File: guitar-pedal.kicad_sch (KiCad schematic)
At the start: 50 parts, among them J1 USB_OTG, J2 AudioJack2, J3 AudioJack2, J4 Test_Headers, SW1 SW_SPDT, SW2 SW_3PDT, SW3 Boot, SW4 Reset, SW5 SW_Push_SPDT, SW6 SW_Push_SPDT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

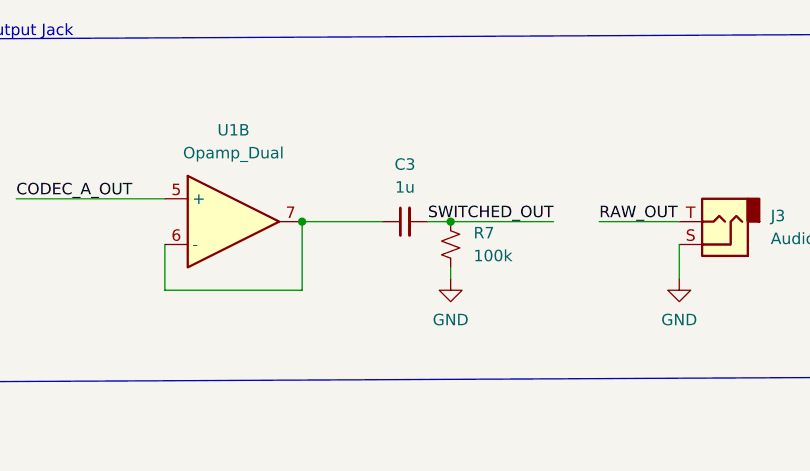
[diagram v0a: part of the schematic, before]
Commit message: add missing letter F from capacitor value
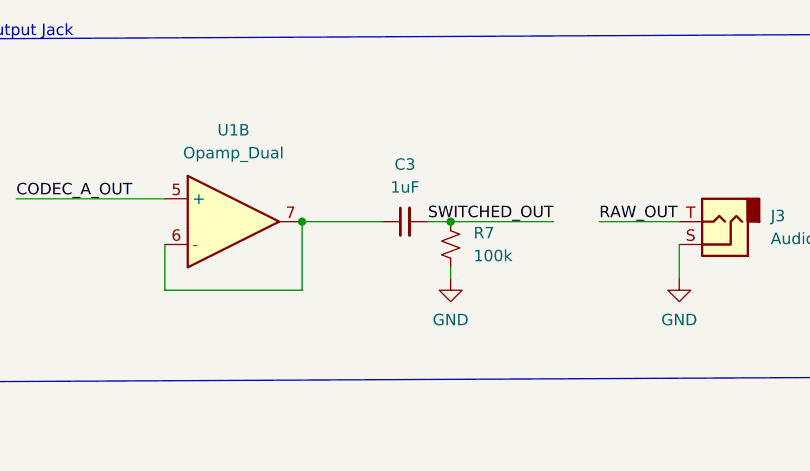
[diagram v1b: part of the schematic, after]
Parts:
- C3: value 1u -> 1uF
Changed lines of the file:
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@@
     (in_bom yes) (on_board yes) (fields_autoplaced)
     (property "Reference" "C3" (id 0) (at 217.1763 38.1 90))
-    (property "Value" "1u" (id 1) (at 217.1763 40.64 90))
+    (property "Value" "1uF" (id 1) (at 217.1763 40.64 90))
     (property "Footprint" "" (id 2) (at 217.17 44.45 0)
       (effects (font (size 1.27 1.27)) hide)
@@
     )
     (path "/5098fff7-b1bd-4ef1-99fe-3f3750157a32"
-      (reference "C3") (unit 1) (value "1u") (footprint "")
+      (reference "C3") (unit 1) (value "1uF") (footprint "")
     )
     (path "/2b35be39-6c74-45b8-a4e7-272df3c08333"

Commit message: some reorganization
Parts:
- gave numbers to parts that had none: 1
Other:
- moved on the sheet: C1, C10, C12, C15, C16, C17, C18, C19, C20, C21, C22, C23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

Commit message: assign footprints and fix a couple small things
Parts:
- C1, C11, C12, C13, C14, C16, C18, C19, C20, C22, C3, C4, C5, C7, C8: footprint (none) -> Capacitor_SMD:C_0603_1608Metric_Pad1.08x0.95mm_HandSolder
- C10, C9: value 10uF -> 1uF; footprint (none) -> Capacitor_SMD:C_0603_1608Metric_Pad1.08x0.95mm_HandSolder
- C15, C17, C6: footprint (none) -> Capacitor_SMD:C_0805_2012Metric_Pad1.18x1.45mm_HandSolder
- C21: value 4.7uF -> 1uF; footprint (none) -> Capacitor_SMD:C_0603_1608Metric_Pad1.08x0.95mm_HandSolder; symbol Device:C_Polarized_Small_US -> Device:C_Small
- C23: footprint (none) -> Capacitor_SMD:C_0805_2012Metric_Pad1.18x1.45mm_HandSolder; symbol Device:C_Small -> Device:C_Polarized_Small_US
- C24: footprint (none) -> Capacitor_SMD:C_0603_1608Metric_Pad1.08x0.95mm_HandSolder; symbol Device:C_Small -> Device:C_Polarized_Small_US
- D1, POT1, POT2, POT3, POT4, POT5, POT6, SW1, SW5, SW6: footprint (none) -> Connector_PinHeader_2.54mm:PinHeader_1x03_P2.54mm_Vertical
- J1: footprint (none) -> Connector_USB:USB_Micro-B_Molex-105017-0001
- J2, J3, SW4: footprint (none) -> Connector_PinHeader_2.54mm:PinHeader_1x02_P2.54mm_Vertical
- J4: footprint (none) -> Connector_PinHeader_2.54mm:PinHeader_1x10_P2.54mm_Vertical
- R1, R3, R5, R7, R9, SW3: footprint (none) -> Resistor_SMD:R_0603_1608Metric_Pad0.98x0.95mm_HandSolder
- R8: footprint (none) -> Resistor_SMD:R_0805_2012Metric_Pad1.20x1.40mm_HandSolder
- SW2: footprint (none) -> Connector_PinHeader_2.54mm:PinHeader_1x09_P2.54mm_Vertical
- U1: footprint (none) -> RC4580IPWR:PW8
- U4: renamed from PCM3002E1; footprint (none) -> PCM3002E:PCM3002E
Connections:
- net +3V3: now also C23.1; no longer C23.2
- net GND: now also C23.2; no longer C23.1

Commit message: getting started on layout
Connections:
- net GND: now also J2.1 (S), J3.1 (S); no longer J2.S, J3.S
- net RAW_IN: now also J2.2 (T); no longer J2.T
- net RAW_OUT: now also J3.2 (T); no longer J3.T
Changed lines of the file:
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@@
     (effects (font (size 1.27 1.27)) (justify left bottom))
   )
-  (symbol (lib_id "Connector:AudioJack2") (at 67.945 36.83 90) (mirror x) (unit 1)
-    (in_bom yes) (on_board yes) (fields_autoplaced)
-    (property "Reference" "J2" (id 0) (at 71.755 34.9249 90)
-      (effects (font (size 1.27 1.27)) (justify right))
-    )
-    (property "Value" "AudioJack2" (id 1) (at 71.755 37.4649 90)
+  (symbol (lib_name "AudioJack2_1") (lib_id "Connector:AudioJack2") (at 67.945 36.83 90) (mirror x) (unit 1)
+    (in_bom yes) (on_board yes)
+    (property "Reference" "J2" (id 0) (at 66.802 29.464 90)
+      (effects (font (size 1.27 1.27)) (justify right))
+    )
+    (property "Value" "AudioJack2" (id 1) (at 62.484 31.496 90)
       (effects (font (size 1.27 1.27)) (justify right))
     )
@@
       (effects (font (size 1.27 1.27)) hide)
     )
-    (pin "S")
-    (pin "T")
+    (pin "2")
+    (pin "1")
   )
   (symbol (lib_id "Switch:SW_Push") (at 271.78 105.918 0) (unit 1)
@@
   )
   (symbol (lib_id "Connector:AudioJack2") (at 255.905 44.45 180) (unit 1)
-    (in_bom yes) (on_board yes) (fields_autoplaced)
-    (property "Reference" "J3" (id 0) (at 260.985 43.8149 0)
-      (effects (font (size 1.27 1.27)) (justify right))
-    )
-    (property "Value" "AudioJack2" (id 1) (at 260.985 46.3549 0)
+    (in_bom yes) (on_board yes)
+    (property "Reference" "J3" (id 0) (at 254.762 38.1 0)
+      (effects (font (size 1.27 1.27)) (justify right))
+    )
+    (property "Value" "AudioJack2" (id 1) (at 250.444 40.132 0)
       (effects (font (size 1.27 1.27)) (justify right))
     )
@@
       (effects (font (size 1.27 1.27)) hide)
     )
-    (pin "S")
-    (pin "T")
+    (pin "1")
+    (pin "2")
   )
   (symbol (lib_id "power:+3V3") (at 238.506 103.632 0) (unit 1)

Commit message: no seriously, get started on layout
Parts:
- J4: footprint Connector_PinHeader_2.54mm:PinHeader_1x10_P2.54mm_Vertical -> Connector_PinHeader_2.54mm:PinHeader_2x05_P2.54mm_Vertical
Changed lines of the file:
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@@
       (effects (font (size 1.27 1.27)) (justify right))
     )
-    (property "Footprint" "Connector_PinHeader_2.54mm:PinHeader_1x10_P2.54mm_Vertical" (id 2) (at 346.202 91.948 0)
+    (property "Footprint" "Connector_PinHeader_2.54mm:PinHeader_2x05_P2.54mm_Vertical" (id 2) (at 346.202 91.948 0)
       (effects (font (size 1.27 1.27)) hide)
     )
@@
     )
     (path "/8b87fcfc-4d33-4e63-b56b-68b24da21f98"
-      (reference "J4") (unit 1) (value "Test_Headers") (footprint "Connector_PinHeader_2.54mm:PinHeader_1x10_P2.54mm_Vertical")
+      (reference "J4") (unit 1) (value "Test_Headers") (footprint "Connector_PinHeader_2.54mm:PinHeader_2x05_P2.54mm_Vertical")
     )
     (path "/d150c883-e641-4548-a17d-a4c8e8775a90"

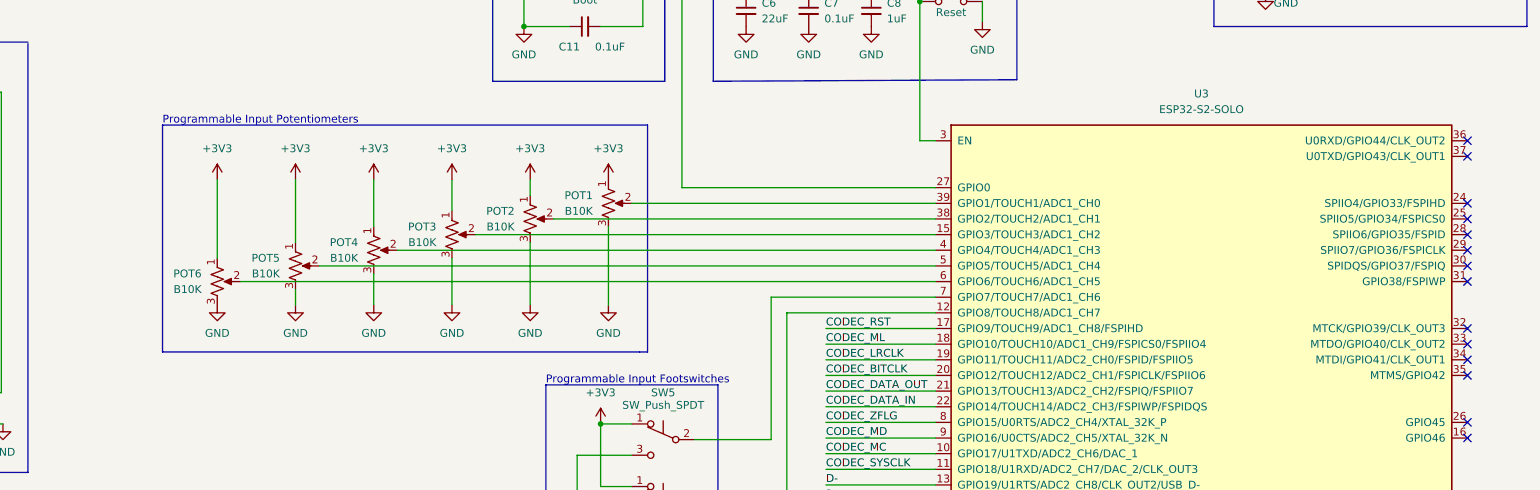
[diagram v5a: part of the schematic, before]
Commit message: Reassign potentiometer pins to esp32
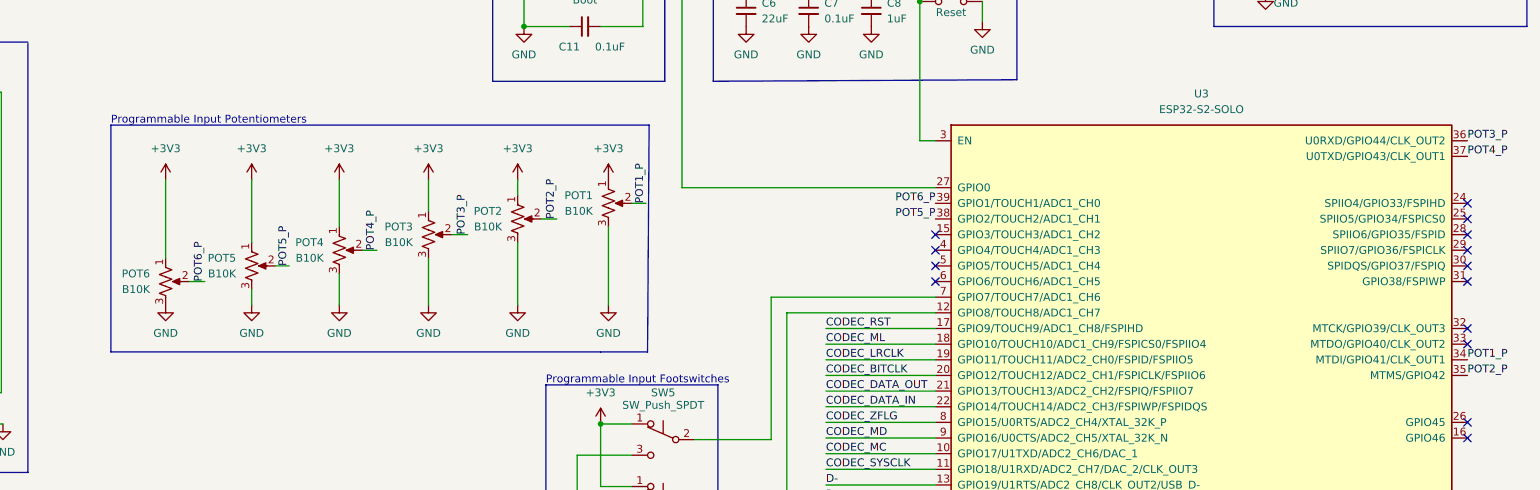
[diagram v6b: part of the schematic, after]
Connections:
- net at U3.4 (GPIO4/TOUCH4/ADC1_CH3): no longer POT4.2
- net at U3.15 (GPIO3/TOUCH3/ADC1_CH2): no longer POT3.2
- net at U3.6 (GPIO6/TOUCH6/ADC1_CH5): no longer POT6.2
- net POT1_P: now reaches POT1.2
- net POT1_P: now also U3.34 (MTDI/GPIO41/CLK_OUT1); no longer U3.39 (GPIO1/TOUCH1/ADC1_CH0)
- net POT2_P: now reaches U3.35 (MTMS/GPIO42)
- net POT2_P: now also POT2.2
- net POT3_P: now reaches U3.36 (U0RXD/GPIO44/CLK_OUT2)
- net POT3_P: now also POT3.2
- net POT4_P: now reaches U3.37 (U0TXD/GPIO43/CLK_OUT1)
- net POT4_P: now also POT4.2
- net POT5_P: now reaches U3.38 (GPIO2/TOUCH2/ADC1_CH1)
- net POT5_P: now also POT5.2; no longer POT2.2
- net at U3.5 (GPIO5/TOUCH5/ADC1_CH4): no longer POT5.2
- new net POT6_P: POT6.2, U3.39 (GPIO1/TOUCH1/ADC1_CH0)
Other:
- moved on the sheet: POT2, POT3, POT4, POT5, POT6

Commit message: layout progress!
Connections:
- net CODEC_BITCLK: now also U3.18 (GPIO10/TOUCH10/ADC1_CH9/FSPICS0/FSPIIO4); no longer U3.20 (GPIO12/TOUCH12/ADC2_CH1/FSPICLK/FSPIIO6)
- net CODEC_DATA_IN: now also U3.11 (GPIO18/U1RXD/ADC2_CH7/DAC_2/CLK_OUT3); no longer U3.22 (GPIO14/TOUCH14/ADC2_CH3/FSPIWP/FSPIDQS)
- net CODEC_DATA_OUT: now also U3.17 (GPIO9/TOUCH9/ADC1_CH8/FSPIHD); no longer U3.21 (GPIO13/TOUCH13/ADC2_CH2/FSPIQ/FSPIIO7)
- net CODEC_MC: now also U3.8 (GPIO15/U0RTS/ADC2_CH4/XTAL_32K_P); no longer U3.10 (GPIO17/U1TXD/ADC2_CH6/DAC_1)
- net CODEC_ML: now also U3.21 (GPIO13/TOUCH13/ADC2_CH2/FSPIQ/FSPIIO7); no longer U3.18 (GPIO10/TOUCH10/ADC1_CH9/FSPICS0/FSPIIO4)
- net CODEC_RST: now also U3.22 (GPIO14/TOUCH14/ADC2_CH3/FSPIWP/FSPIDQS); no longer U3.17 (GPIO9/TOUCH9/ADC1_CH8/FSPIHD)
- net CODEC_SYSCLK: now also U3.20 (GPIO12/TOUCH12/ADC2_CH1/FSPICLK/FSPIIO6); no longer U3.11 (GPIO18/U1RXD/ADC2_CH7/DAC_2/CLK_OUT3)
- net CODEC_ZFLG: now also U3.10 (GPIO17/U1TXD/ADC2_CH6/DAC_1); no longer U3.8 (GPIO15/U0RTS/ADC2_CH4/XTAL_32K_P)
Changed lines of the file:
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@@
     (effects (font (size 1.27 1.27)) (justify right bottom))
   )
-  (label "POT3_P" (at 193.294 143.764 90)
+  (label "CODEC_LRCLK" (at 251.46 164.084 0)
     (effects (font (size 1.27 1.27)) (justify left bottom))
   )
-  (label "CODEC_ZFLG" (at 251.46 174.244 0)
+  (label "POT3_P" (at 193.294 143.764 90)
     (effects (font (size 1.27 1.27)) (justify left bottom))
   )
@@
     (effects (font (size 1.27 1.27)) (justify left bottom))
   )
-  (label "CODEC_A_OUT" (at 323.342 86.868 0)
+  (label "CODEC_BITCLK" (at 251.46 161.544 0)
     (effects (font (size 1.27 1.27)) (justify left bottom))
   )
-  (label "CODEC_BITCLK" (at 251.46 166.624 0)
+  (label "CODEC_A_OUT" (at 323.342 86.868 0)
     (effects (font (size 1.27 1.27)) (justify left bottom))
   )
@@
   )
   (label "SWITCHED_OUT" (at 339.344 43.18 0)
+    (effects (font (size 1.27 1.27)) (justify left bottom))
+  )
+  (label "CODEC_MC" (at 251.46 174.244 0)
+    (effects (font (size 1.27 1.27)) (justify left bottom))
+  )
+  (label "CODEC_DATA_IN" (at 251.46 181.864 0)
     (effects (font (size 1.27 1.27)) (justify left bottom))
   )
@@
     (effects (font (size 1.27 1.27)) (justify left bottom))
   )
-  (label "CODEC_ML" (at 251.46 161.544 0)
+  (label "CODEC_ZFLG" (at 251.46 179.324 0)
     (effects (font (size 1.27 1.27)) (justify left bottom))
   )
@@
     (effects (font (size 1.27 1.27)) (justify right bottom))
   )
-  (label "CODEC_MC" (at 251.46 179.324 0)
-    (effects (font (size 1.27 1.27)) (justify left bottom))
-  )
   (label "POT2_P" (at 355.6 166.624 0)
     (effects (font (size 1.27 1.27)) (justify left bottom))
   )
-  (label "CODEC_LRCLK" (at 251.46 164.084 0)
+  (label "CODEC_RST" (at 251.46 171.704 0)
     (effects (font (size 1.27 1.27)) (justify left bottom))
   )
@@
     (effects (font (size 1.27 1.27)) (justify left bottom))
   )
-  (label "CODEC_DATA_OUT" (at 251.46 169.164 0)
-    (effects (font (size 1.27 1.27)) (justify left bottom))
-  )
-  (label "CODEC_SYSCLK" (at 251.46 181.864 0)
-    (effects (font (size 1.27 1.27)) (justify left bottom))
-  )
   (label "POT1_P" (at 222.25 138.684 90)
     (effects (font (size 1.27 1.27)) (justify left bottom))
@@
     (effects (font (size 1.27 1.27)) (justify left bottom))
   )
-  (label "CODEC_RST" (at 251.46 159.004 0)
+  (label "CODEC_DATA_OUT" (at 251.46 159.004 0)
     (effects (font (size 1.27 1.27)) (justify left bottom))
   )
   (label "D-" (at 251.46 184.404 0)
-    (effects (font (size 1.27 1.27)) (justify left bottom))
-  )
-  (label "CODEC_DATA_IN" (at 251.46 171.704 0)
     (effects (font (size 1.27 1.27)) (justify left bottom))
   )
@@
     (effects (font (size 1.27 1.27)) (justify left bottom))
   )
+  (label "CODEC_SYSCLK" (at 251.46 166.624 0)
+    (effects (font (size 1.27 1.27)) (justify left bottom))
+  )
   (label "D+" (at 42.418 44.704 180)
     (effects (font (size 1.27 1.27)) (justify right bottom))
@@
     (effects (font (size 1.27 1.27)) (justify left bottom))
   )
+  (label "CODEC_ML" (at 251.46 169.164 0)
+    (effects (font (size 1.27 1.27)) (justify left bottom))
+  )

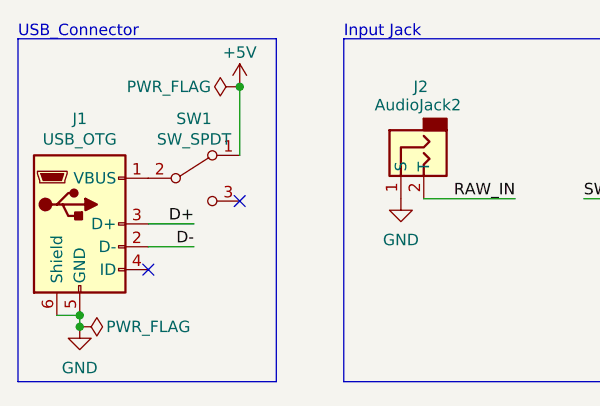
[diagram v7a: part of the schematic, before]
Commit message: Fix switch to ground
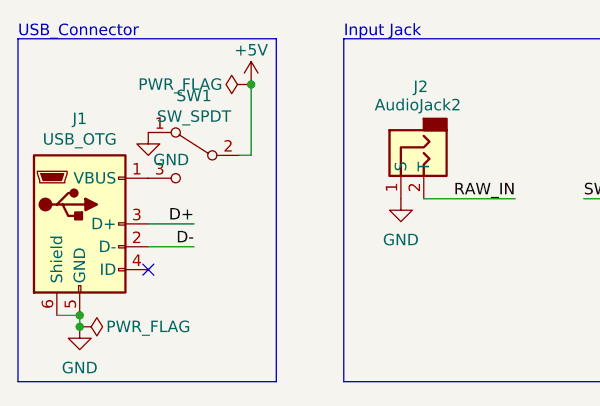
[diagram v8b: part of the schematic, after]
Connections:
- net +5V: now also SW1.2 (B); no longer SW1.1 (A)
- net GND: now also SW1.1 (A)
- net at J1.1 (VBUS): now also SW1.3 (C); no longer SW1.2 (B)
- no-connect marks 19 -> 18
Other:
- moved on the sheet: SW1
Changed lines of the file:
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@@
   (junction (at 248.666 103.632) (diameter 0) (color 0 0 0 0)
   )
+  (junction (at 48.768 29.21) (diameter 0) (color 0 0 0 0)
+  )
   (junction (at 103.632 174.498) (diameter 0) (color 0 0 0 0)
   )
@@
   )
   (junction (at 266.7 105.918) (diameter 0) (color 0 0 0 0)
-  )
-  (junction (at 47.498 29.464) (diameter 0) (color 0 0 0 0)
   )
   (junction (at 52.07 125.73) (diameter 0) (color 0 0 0 0)
@@
   (no_connect (at 355.6 176.784))
   (no_connect (at 355.6 161.544))
-  (no_connect (at 47.498 42.164))
   (no_connect (at 269.24 143.764))
   (wire (pts (xy 269.24 153.924) (xy 242.57 153.924))
@@
     (stroke (width 0) (type default) (color 0 0 0 0))
   )
+  (wire (pts (xy 47.498 37.084) (xy 48.768 37.084))
+    (stroke (width 0) (type default) (color 0 0 0 0))
+  )
   (wire (pts (xy 34.798 142.748) (xy 53.848 142.748))
     (stroke (width 0) (type default) (color 0 0 0 0))
@@
     (stroke (width 0) (type default) (color 0 0 0 0))
   )
+  (wire (pts (xy 48.768 37.084) (xy 48.768 29.21))
+    (stroke (width 0) (type default) (color 0 0 0 0))
+  )
   (wire (pts (xy 193.675 46.99) (xy 193.675 52.07))
     (stroke (width 0) (type default) (color 0 0 0 0))
@@
     (stroke (width 0) (type default) (color 0 0 0 0))
   )
+  (wire (pts (xy 37.338 44.704) (xy 42.418 44.704))
+    (stroke (width 0) (type default) (color 0 0 0 0))
+  )
   (wire (pts (xy 106.045 41.91) (xy 103.505 41.91))
     (stroke (width 0) (type default) (color 0 0 0 0))
@@
     (stroke (width 0) (type default) (color 0 0 0 0))
   )
-  (wire (pts (xy 37.338 44.704) (xy 42.418 44.704))
-    (stroke (width 0) (type default) (color 0 0 0 0))
-  )
   (wire (pts (xy 322.834 104.648) (xy 341.122 104.648))
     (stroke (width 0) (type default) (color 0 0 0 0))
@@
     (stroke (width 0) (type default) (color 0 0 0 0))
   )
-  (wire (pts (xy 47.244 29.464) (xy 47.498 29.464))
+  (wire (pts (xy 48.514 29.21) (xy 48.768 29.21))
     (stroke (width 0) (type default) (color 0 0 0 0))
   )
@@
   )
   (polyline (pts (xy 314.452 76.454) (xy 365.252 76.454))
-    (stroke (width 0) (type default) (color 0 0 0 0))
-  )
-  (wire (pts (xy 47.498 29.464) (xy 47.498 37.084))
     (stroke (width 0) (type default) (color 0 0 0 0))
   )
@@
     (pin "1")
   )
-  (symbol (lib_id "Switch:SW_SPDT") (at 42.418 39.624 0) (unit 1)
-    (in_bom yes) (on_board yes)
-    (property "Reference" "SW1" (id 0) (at 42.418 33.02 0))
-    (property "Value" "SW_SPDT" (id 1) (at 42.418 35.306 0))
-    (property "Footprint" "Connector_PinHeader_2.54mm:PinHeader_1x03_P2.54mm_Vertical" (id 2) (at 42.418 39.624 0)
-      (effects (font (size 1.27 1.27)) hide)
-    )
-    (property "Datasheet" "~" (id 3) (at 42.418 39.624 0)
+  (symbol (lib_id "Switch:SW_SPDT") (at 42.418 37.084 0) (mirror y) (unit 1)
+    (in_bom yes) (on_board yes)
+    (property "Reference" "SW1" (id 0) (at 42.418 30.48 0))
+    (property "Value" "SW_SPDT" (id 1) (at 42.418 32.766 0))
+    (property "Footprint" "Connector_PinHeader_2.54mm:PinHeader_1x03_P2.54mm_Vertical" (id 2) (at 42.418 37.084 0)
+      (effects (font (size 1.27 1.27)) hide)
+    )
+    (property "Datasheet" "~" (id 3) (at 42.418 37.084 0)
       (effects (font (size 1.27 1.27)) hide)
     )
@@
     (pin "3")
   )
-  (symbol (lib_id "power:+5V") (at 47.498 29.464 0) (unit 1)
-    (in_bom yes) (on_board yes)
-    (property "Reference" "#PWR0128" (id 0) (at 47.498 33.274 0)
-      (effects (font (size 1.27 1.27)) hide)
-    )
-    (property "Value" "+5V" (id 1) (at 47.498 25.654 0))
-    (property "Footprint" "" (id 2) (at 47.498 29.464 0)
-      (effects (font (size 1.27 1.27)) hide)
-    )
-    (property "Datasheet" "" (id 3) (at 47.498 29.464 0)
+  (symbol (lib_id "power:+5V") (at 48.768 29.21 0) (unit 1)
+    (in_bom yes) (on_board yes)
+    (property "Reference" "#PWR0128" (id 0) (at 48.768 33.02 0)
+      (effects (font (size 1.27 1.27)) hide)
+    )
+    (property "Value" "+5V" (id 1) (at 48.768 25.4 0))
+    (property "Footprint" "" (id 2) (at 48.768 29.21 0)
+      (effects (font (size 1.27 1.27)) hide)
+    )
+    (property "Datasheet" "" (id 3) (at 48.768 29.21 0)
       (effects (font (size 1.27 1.27)) hide)
     )
@@
     (pin "2")
   )
-  (symbol (lib_id "power:PWR_FLAG") (at 47.244 29.464 90) (mirror x) (unit 1)
-    (in_bom yes) (on_board yes)
-    (property "Reference" "#FLG0101" (id 0) (at 45.339 29.464 0)
-      (effects (font (size 1.27 1.27)) hide)
-    )
-    (property "Value" "PWR_FLAG" (id 1) (at 39.624 29.464 90))
-    (property "Footprint" "" (id 2) (at 47.244 29.464 0)
-      (effects (font (size 1.27 1.27)) hide)
-    )
-    (property "Datasheet" "~" (id 3) (at 47.244 29.464 0)
+  (symbol (lib_id "power:PWR_FLAG") (at 48.514 29.21 90) (mirror x) (unit 1)
+    (in_bom yes) (on_board yes)
+    (property "Reference" "#FLG0101" (id 0) (at 46.609 29.21 0)
+      (effects (font (size 1.27 1.27)) hide)
+    )
+    (property "Value" "PWR_FLAG" (id 1) (at 40.894 29.21 90))
+    (property "Footprint" "" (id 2) (at 48.514 29.21 0)
+      (effects (font (size 1.27 1.27)) hide)
+    )
+    (property "Datasheet" "~" (id 3) (at 48.514 29.21 0)
       (effects (font (size 1.27 1.27)) hide)
     )
@@
     )
     (property "Datasheet" "" (id 3) (at 172.466 134.874 0)
+      (effects (font (size 1.27 1.27)) hide)
+    )
+    (pin "1")
+  )
+  (symbol (lib_id "power:GND") (at 37.338 34.544 0) (unit 1)
+    (in_bom yes) (on_board yes)
+    (property "Reference" "#PWR?" (id 0) (at 37.338 40.894 0)
+      (effects (font (size 1.27 1.27)) hide)
+    )
+    (property "Value" "GND" (id 1) (at 39.878 37.592 0))
+    (property "Footprint" "" (id 2) (at 37.338 34.544 0)
+      (effects (font (size 1.27 1.27)) hide)
+    )
+    (property "Datasheet" "" (id 3) (at 37.338 34.544 0)
       (effects (font (size 1.27 1.27)) hide)
     )
@@
       (reference "#PWR0137") (unit 1) (value "+3V3") (footprint "")
     )
+    (path "/a9104608-e87f-4050-9bf2-8dd959f138c7"
+      (reference "#PWR?") (unit 1) (value "GND") (footprint "")
+    )
     (path "/75668013-1e69-49e1-87ea-b4703c0a1350"
